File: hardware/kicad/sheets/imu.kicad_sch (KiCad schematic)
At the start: 5 parts, among them U19 LSM6DSOXTR

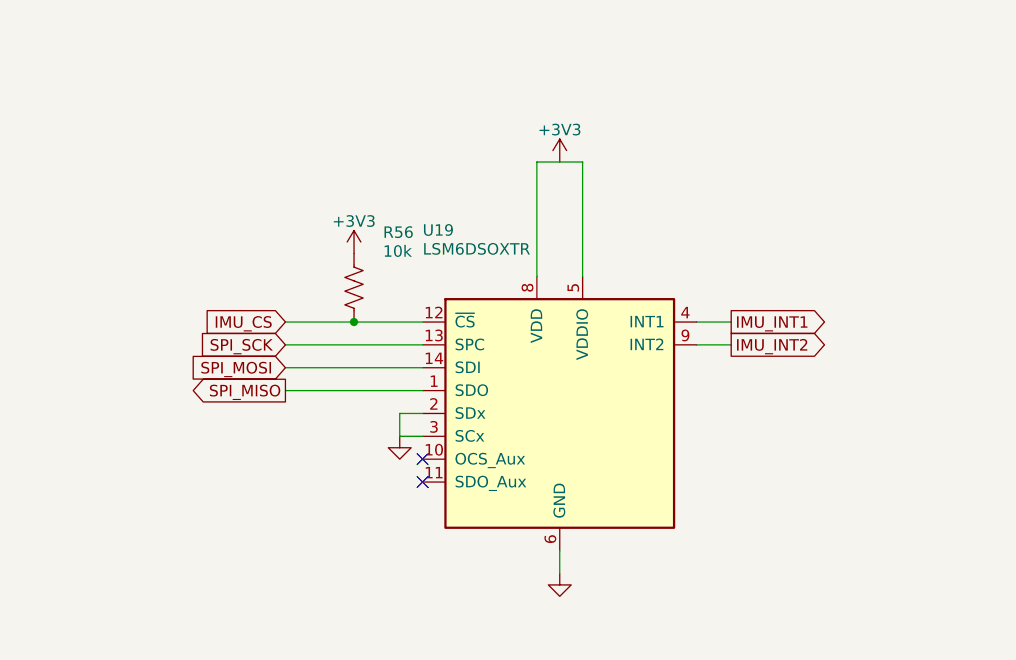
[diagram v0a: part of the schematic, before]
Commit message: Put supply pins on top and grounds on the bottom of IC symbols; flake8-clean Python
Schematic: re-laid out pins on U2, U3, U6, U7, U11, U14, U17-U20, U22-U24
and PS1 (supply on top, ground/strap pins on the bottom edge) via custom
`cryocooler:` symbols (make_lib.from_stock) and a gnd_bus helper; U18/U2
use mirroring instead of a 180 degree rotation. Nets are unchanged (ERC 0,
117/117 datasheet rules, PCB nets still match). Text placement now shows
every power-symbol name, avoids wires, and uses a realistic character width.

Python: black -l 79 -S plus manual wrapping so hardware/kicad and scripts/
pass flake8; add .flake8.

Co-Authored-By: Claude Sonnet 5.5 <noreply@anthropic.com>
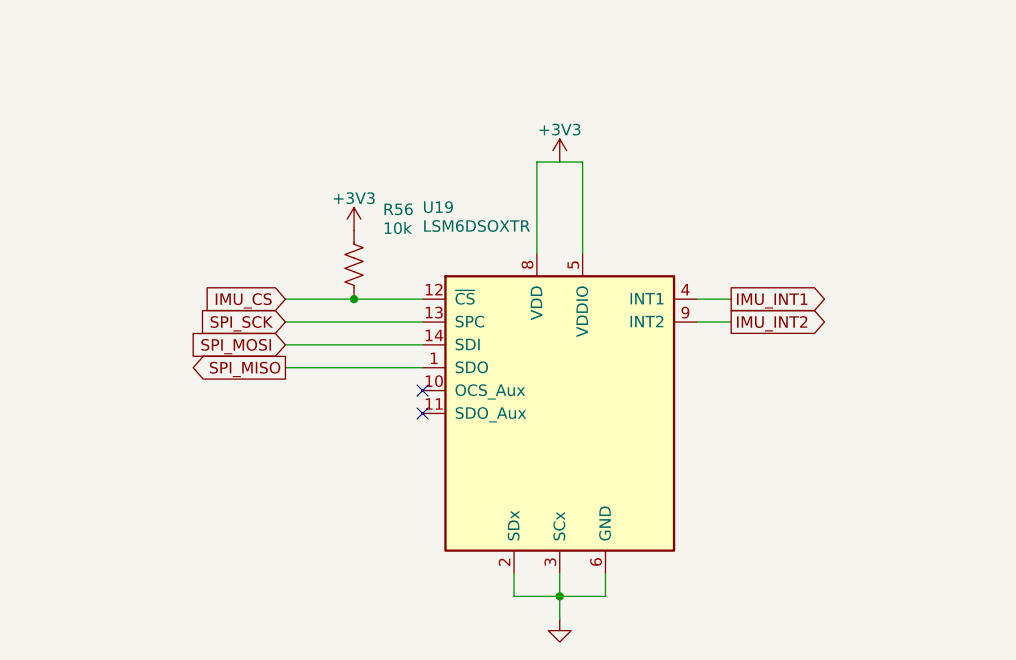
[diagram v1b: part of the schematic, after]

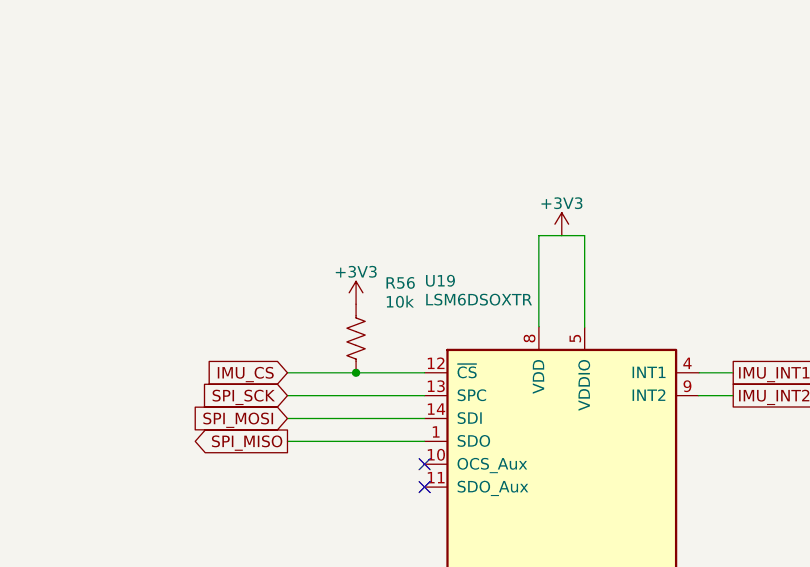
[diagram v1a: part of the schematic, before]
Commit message: KiCad schematic: INA239, ADS1220, SC18IS604 bridge, relay driver, test points
- system_current: INA237 -> INA239 (SPI, CS GPIO3) with the 49.9 ohm / 470 nF
  input filter, power LED and ALERT LED; VBUS shares the filtered IN- node.
- cold_head: ADS122C04 -> ADS1220 (SPI, CS GPIO44).
- i2c_bridge (new): SC18IS604 SPI-to-I2C bridge for the EMC2303, with a
  74LVC1G125 gating its MISO onto the shared bus.
- compressor_relay (new): GPIO16 high-side switch sharing one generator
  function with the amplifier REM switch.
- debug (new): about 40 test points and rail LEDs (the isolated rail LED
  returns to ISO_GND).
- ISO7741 -> ACS37800 SPI lines are straight wires (pins reordered on the
  symbol); USB_VBUS is one wire plus a naming label.
- Custom symbols for INA239, ADS1220, SC18IS604; datasheet rules 117 -> 162;
  GPIO map checks updated. ERC 0.

Co-Authored-By: Claude Sonnet 5.5 <noreply@anthropic.com>
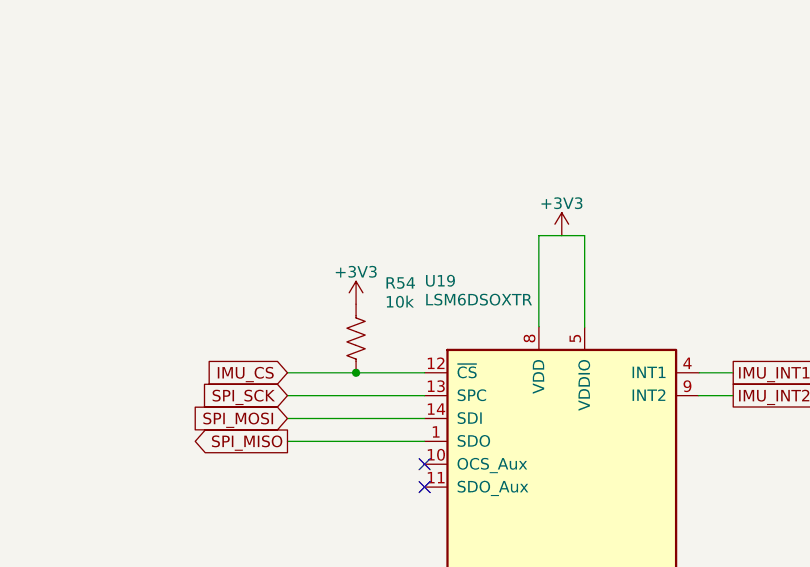
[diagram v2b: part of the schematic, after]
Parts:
- removed R56: 10k, Resistor_SMD:R_0603_1608Metric, symbol Device:R_US
- added R54: 10k, Resistor_SMD:R_0603_1608Metric, symbol Device:R_US
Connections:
- net +3V3: now also R54.1
- net IMU_CS: now also R54.2

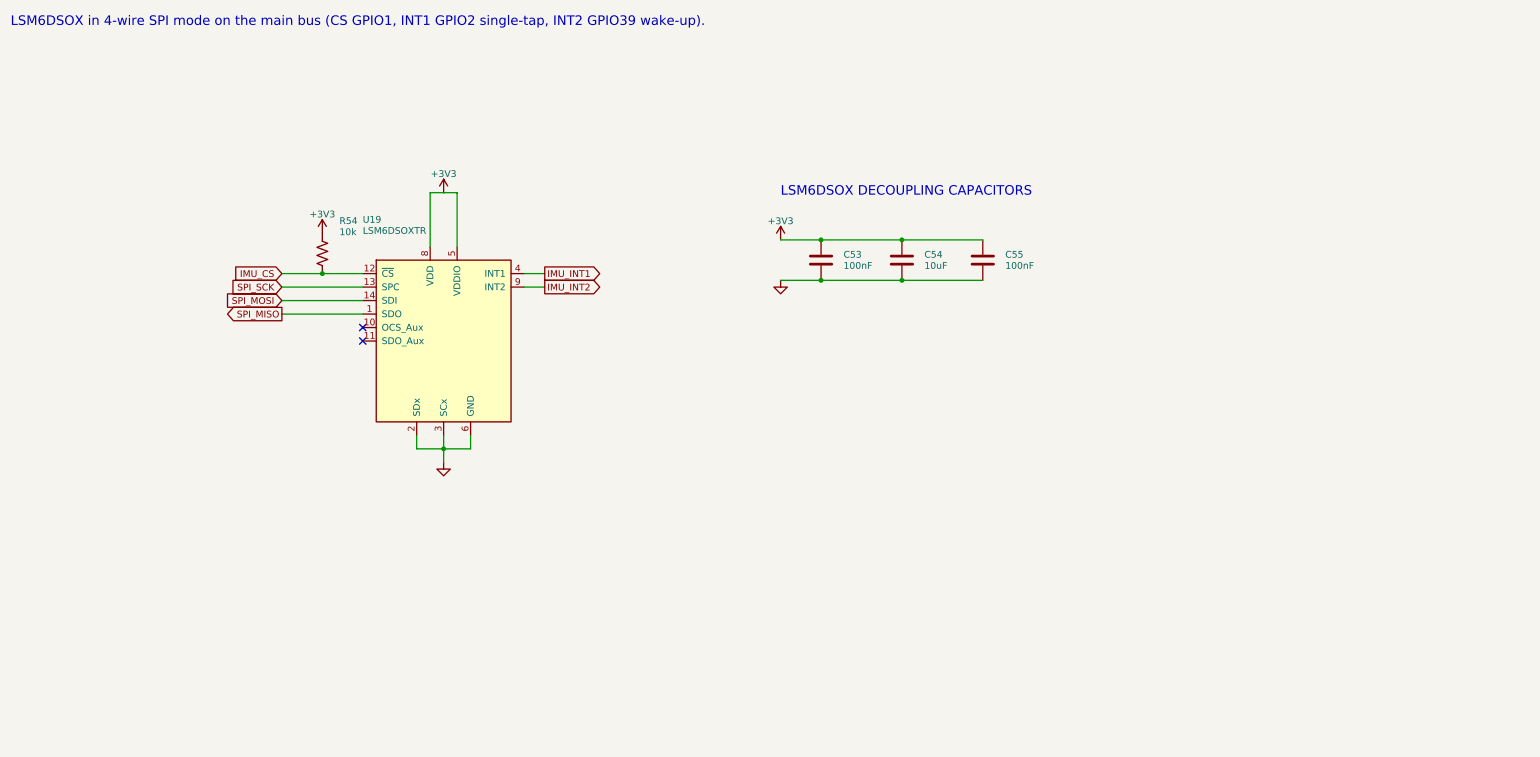
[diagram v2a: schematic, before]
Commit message: Move the IMU off-board (J14) and add labelled module boxes to the PCB
The LSM6DSOX is now the Adafruit breakout (product 4438) mounted on the
cryocooler and cabled to a 10-pin JST XH header (J14) over the shared SPI
bus. U19 and its capacitors are gone; J14 and six 100 R series resistors
are added, and every other reference number is unchanged.

PCB (130 x 110 mm, was 130 x 100):
- one outlined, labelled silkscreen box per module (pcbfloorplan.py); the
  placer keeps parts inside their box and reserves a label pocket beside
  every part so each label sits next to its own part
- box 3D models for U3, L2, L3, F1 and PS1, whose library models are missing
- re-routed; DRC 0 errors, 0 unconnected; back logo recentred
- gen_pcb.py texts redoes the silkscreen on a routed board

Firmware: SPI clock constant for the module, comments updated; ambient
temperature now reads the cooler-body IMU temperature.

Docs, BOM and fabrication files regenerated.

Co-Authored-By: Claude Sonnet 5.5 <noreply@anthropic.com>
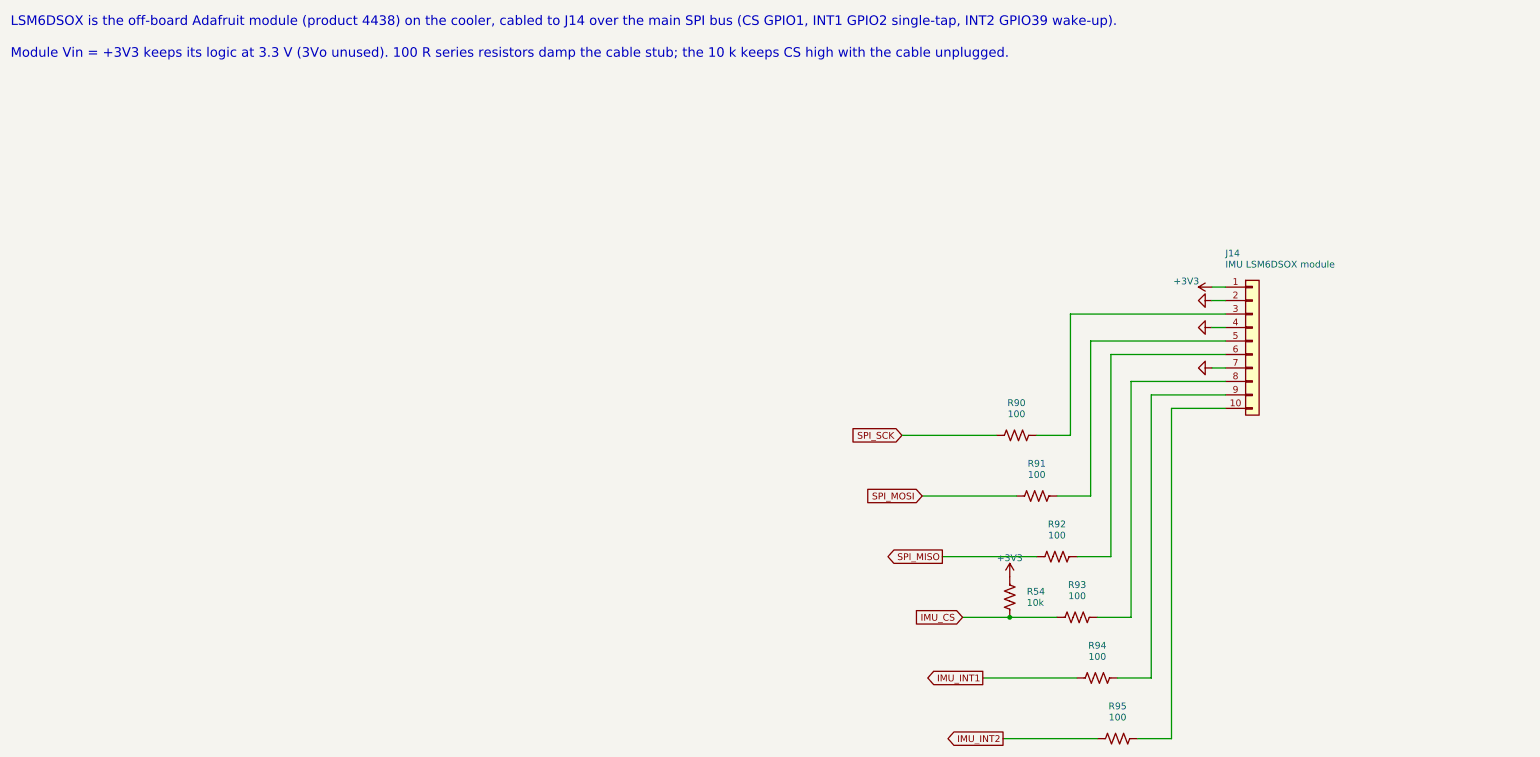
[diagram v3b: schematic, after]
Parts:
- added R90, R94, R95: 100, Resistor_SMD:R_0603_1608Metric, symbol Device:R_US
- J14: renamed from U19; value LSM6DSOXTR -> IMU LSM6DSOX module; footprint Package_LGA:LGA-14_3x2.5mm_P0.5mm_LayoutBorder3x4y -> Connector_JST:JST_XH_B10B-XH-A_1x10_P2.50mm_Vertical; symbol cryocooler:LSM6DSOXTR -> Connector_Generic:Conn_01x10
- R91: renamed from C53; value 100nF -> 100; footprint Capacitor_SMD:C_0603_1608Metric -> Resistor_SMD:R_0603_1608Metric; symbol Device:C -> Device:R_US
- R92: renamed from C54; value 10uF -> 100; footprint Capacitor_SMD:C_0805_2012Metric -> Resistor_SMD:R_0603_1608Metric; symbol Device:C -> Device:R_US
- R93: renamed from C55; value 100nF -> 100; footprint Capacitor_SMD:C_0603_1608Metric -> Resistor_SMD:R_0603_1608Metric; symbol Device:C -> Device:R_US
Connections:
- net +3V3: now also J14.1 (Pin_1); no longer J14.5 (VDDIO), J14.8 (VDD), R91.1, R92.1, R93.1
- net GND: now also J14.4 (Pin_4); no longer J14.3 (SCx), J14.6 (GND), R91.2, R92.2, R93.2
- net IMU_CS: now also R93.1; no longer J14.12 (~{CS})
- net IMU_INT1: now also R94.1; no longer J14.4 (INT1)
- net IMU_INT2: now also R95.1; no longer J14.9 (INT2)
- net SPI_MISO: now also R92.1; no longer J14.1 (SDO)
- net SPI_MOSI: now also R91.1; no longer J14.14 (SDI)
- net SPI_SCK: now also R90.1; no longer J14.13 (SPC)
- net at J14.10 (Pin_10): now also R95.2
- new net: J14.3 (Pin_3), R90.2
- new net: J14.5 (Pin_5), R91.2
- new net: J14.6 (Pin_6), R92.2
- new net: J14.8 (Pin_8), R93.2
- new net: J14.9 (Pin_9), R94.2
- no-connect marks 2 -> 0
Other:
- note added: "LSM6DSOX is the off-board Adafruit module (product 4438) on the cooler, cabled to J14 over the main SPI bus (CS GPIO1, INT1 GPIO2 single-tap, INT2 GPIO39 wake-up)."
- note added: "Module Vin = +3V3 keeps its logic at 3.3 V (3Vo unused). 100 R series resistors damp the cable stub; the 10 k keeps CS high with the cable unplugged."
- note removed: "LSM6DSOX DECOUPLING CAPACITORS"
- note removed: "LSM6DSOX in 4-wire SPI mode on the main bus (CS GPIO1, INT1 GPIO2 single-tap, INT2 GPIO39 wake-up)."

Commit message: Add per-section supply jumpers, 8-pin IMU header and connector pin labels
- Four 1.27 mm 2-pin jumpers (JP1-JP4), each with a rail-on LED, cut the
  supply of one section for debugging: signal generator +3V3, +-15V
  generator +5V in, isolated amp-current supply +5V in, and a shared
  +3V3 net for the cooling chips (EMC2303, RTD ADC, I2C bridge).
- J14 is now an 8-pin JST XH in the Adafruit LSM6DSOX pad order
  (VIN, GND, SCL, SDA, DO, CS, I1, I2); firmware pin comments updated.
- Pin-function labels beside every connector, "RAILS ±15V" box title.
- Board re-placed and re-routed (130 x 110 mm); DRC 0 errors, 0 unconnected,
  ERC 0, 173 datasheet rules pass. BOM, READMEs, Gerbers and renders
  regenerated; link_usb_vbus.py now adapts to the routed layout.

Co-Authored-By: Claude Sonnet 5.5 <noreply@anthropic.com>
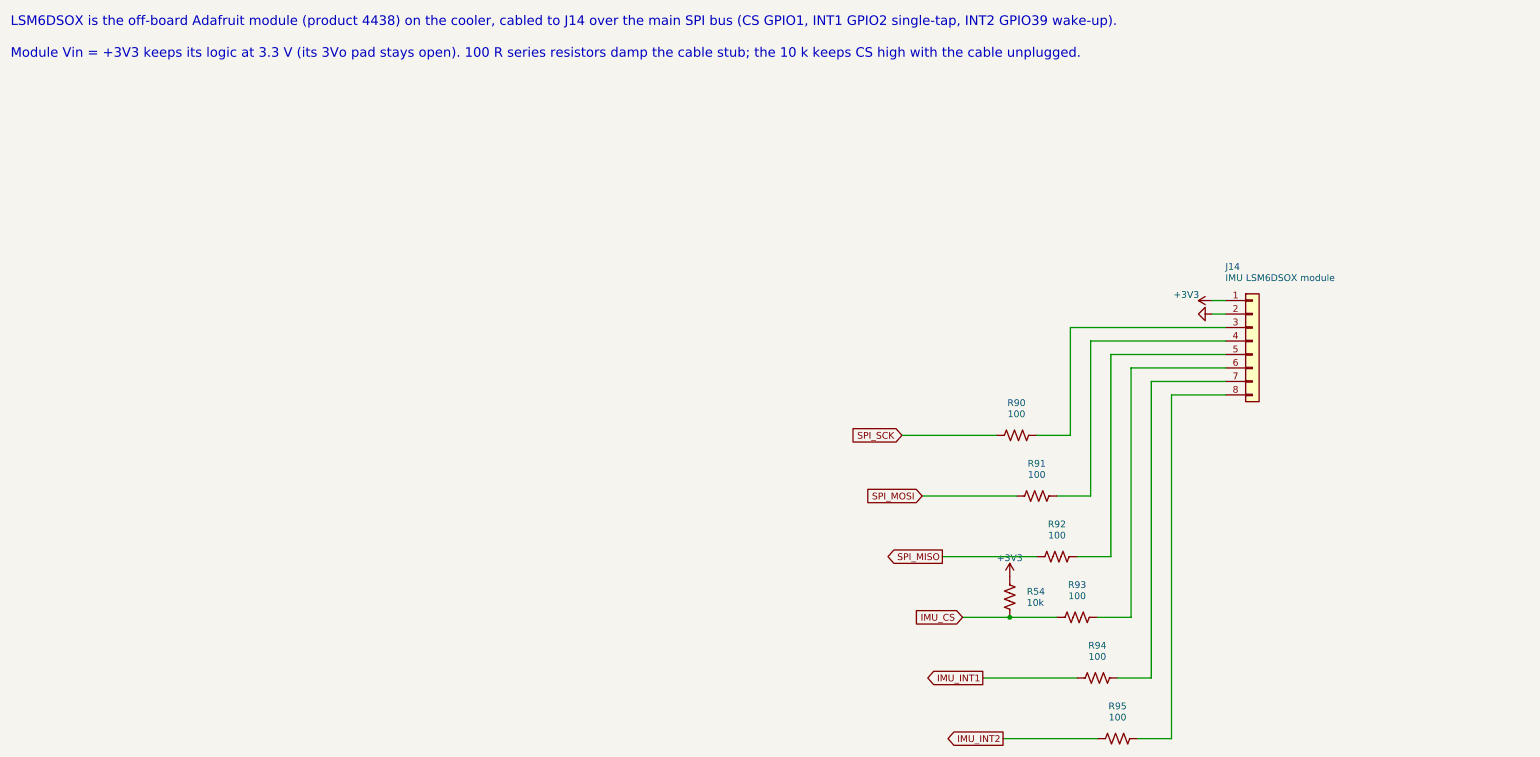
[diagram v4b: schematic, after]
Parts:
- removed R93, R94: 100, Resistor_SMD:R_0603_1608Metric, symbol Device:R_US
- added R90, R91: 100, Resistor_SMD:R_0603_1608Metric, symbol Device:R_US
- J14: footprint Connector_JST:JST_XH_B10B-XH-A_1x10_P2.50mm_Vertical -> Connector_JST:JST_XH_B8B-XH-A_1x08_P2.50mm_Vertical; symbol Connector_Generic:Conn_01x10 -> Connector_Generic:Conn_01x08
- R54: renamed from R92; value 100 -> 10k
- R94: renamed from R54; value 10k -> 100
- renumbered R90 to R92, R91 to R93
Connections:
- net +3V3: now also R54.1; no longer R94.1
- net GND: no longer J14.4 (Pin_4), J14.7 (Pin_7)
- net IMU_CS: now also R54.2, R93.1; no longer R94.2
- net IMU_INT1: now also R94.1
- net SPI_MISO: now also R92.1; no longer R54.1
- net SPI_MOSI: now also R91.1; no longer R93.1
- net SPI_SCK: now also R90.1; no longer R92.1
- net at R95.2: now also J14.8 (Pin_8); no longer J14.10 (Pin_10)
- net at J14.3 (Pin_3): now also R90.2; no longer R92.2
- net at J14.5 (Pin_5): now also R92.2; no longer R93.2
- net at J14.6 (Pin_6): now also R93.2; no longer R54.2
- new net: J14.7 (Pin_7), R94.2
- new net: J14.4 (Pin_4), R91.2
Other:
- note added: "Module Vin = +3V3 keeps its logic at 3.3 V (its 3Vo pad stays open). 100 R series resistors damp the cable stub; the 10 k keeps CS high with the cable unplugged."
- note removed: "Module Vin = +3V3 keeps its logic at 3.3 V (3Vo unused). 100 R series resistors damp the cable stub; the 10 k keeps CS high with the cable unplugged."
- moved on the sheet: R54, R92, R93, R94

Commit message: Replace the ±15 V LDOs with one LT3097 and add a power-good interlock
- rails_15v: ADP7142 + ADP7182 replaced by one LT3097 (±14.7 V, 147 k SET
  resistors); the ADP5071 output caps are now 22 uF / 50 V and double as the
  LT3097 inputs. PGP / PGN make the PG_15V node (fed from +15 V, so it reads
  0 V if a rail is missing).
- amp_control: a series BSS138 (Q9) gated by PG_15V blocks AMP_REM unless
  both rails are good. New power_good sheet: LED (D23) and the active-low
  PG_15V_N flag on GPIO43 (PG_15V_N_PIN).
- Tooling: LT3097 symbol, footprint and 3D envelope; datasheet rules (191),
  GPIO check, BOM tables, floor plan, PAD_BRIDGES and pre-placed GND vias in
  gen_pcb.py, new fix_route.py for post-route clean-up.
- Board regenerated and routed with Freerouting 2.5.0: DRC 0 unconnected,
  0 schematic-parity issues, no copper violations. Gerbers, JLCPCB zip,
  renders, BOM, CPL and schematic PDF regenerated.

Co-Authored-By: Claude Sonnet 5.5 <noreply@anthropic.com>
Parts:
- removed R90, R94: 100, Resistor_SMD:R_0603_1608Metric, symbol Device:R_US
- added R54: 10k, Resistor_SMD:R_0603_1608Metric, symbol Device:R_US
- added R95: 100, Resistor_SMD:R_0603_1608Metric, symbol Device:R_US
- R93: renamed from R54; value 10k -> 100
- renumbered R91 to R90, R92 to R91, R93 to R92, R95 to R94
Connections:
- net +3V3: now also R54.1; no longer R93.1
- net IMU_CS: now also R93.1, R54.2; no longer R92.1, R93.2
- net IMU_INT1: now also R94.1
- net IMU_INT2: now also R95.1; no longer R94.1
- net SPI_MISO: now also R92.1; no longer R91.1
- net SPI_MOSI: now also R91.1; no longer R90.1
- net SPI_SCK: now also R90.1
- net at R94.2: now also J14.7 (Pin_7); no longer J14.8 (Pin_8)
- net at J14.3 (Pin_3): now also R90.2
- net at J14.4 (Pin_4): now also R91.2; no longer R90.2
- net at J14.5 (Pin_5): now also R92.2; no longer R91.2
- net at J14.6 (Pin_6): now also R93.2; no longer R92.2
- new net: J14.8 (Pin_8), R95.2
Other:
- moved on the sheet: R90, R91, R92, R93, R94
